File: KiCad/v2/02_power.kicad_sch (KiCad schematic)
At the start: 1 part, among them IC201 TPS63000DRCR

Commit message: scheme for voltage regulators
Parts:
- added C201, C202, C208, C209: 2.2uF, Capacitor_SMD:C_0603_1608Metric, symbol Device:C
- added C203, C205, C206, C210, C212, C213: 10uF, Capacitor_SMD:C_0603_1608Metric, symbol Device:C
- added C204, C211: 30pF, Capacitor_SMD:C_0603_1608Metric, symbol Device:C
- added C207, C214: 100nF, Capacitor_SMD:C_0603_1608Metric, symbol Device:C
- added C215, C216: 22uF, Capacitor_SMD:C_0603_1608Metric, symbol Device:C
- added D201, D203, D205, D206: 1N5819HW-7-F, Diode_SMD:D_SOD-123, symbol Device:D_Schottky
- added D202, D204: LED, LED_SMD:LED_0603_1608Metric, symbol Device:LED
- added F201, F202: 3A, Fuse:Fuse_0805_2012Metric, symbol Device:Polyfuse
- added FB201, FB202: 120R, Fuse:Fuse_0603_1608Metric, symbol Device:FerriteBead
- added IC202: TPS63000DRCR, psu:TPS63002DRCR, symbol psu:TPS63000DRCR
- added J201: Barrel_Jack_Switch_Pin3Ring, Connector_BarrelJack:BarrelJack_GCT_DCJ200-10-A_Horizontal, symbol Connector:Barrel_Jack_Switch_Pin3Ring
- added J202, J204: Conn_01x03_Pin, Connector_PinHeader_2.54mm:PinHeader_1x03_P2.54mm_Vertical, symbol Connector:Conn_01x03_Pin
- added J203, J205: Conn_02x03_Odd_Even, Connector_PinHeader_2.54mm:PinHeader_2x03_P2.54mm_Vertical, symbol Connector_Generic:Conn_02x03_Odd_Even
- added L201, L202: 2u2H, Inductor_SMD:L_Changjiang_FXL0630, symbol Device:L
- added R201, R205: 1kR, Resistor_SMD:R_0402_1005Metric, symbol Device:R
- added R202, R206: 100R, Resistor_SMD:R_0402_1005Metric, symbol Device:R
- added R203: 900kR, Resistor_SMD:R_0402_1005Metric, symbol Device:R
- added R204, R208: 100kR, Resistor_SMD:R_0402_1005Metric, symbol Device:R
- added R207: 560kR, Resistor_SMD:R_0402_1005Metric, symbol Device:R
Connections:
- net +5V: now reaches IC201.1 (VOUT)
- net +5V: now also C204.1, C205.1, C206.1, J202.1 (Pin_1), J204.1 (Pin_1), R201.2, R203.1
- net 5V_FB: now reaches IC201.10 (FB)
- net 5V_FB: now also C204.2, R203.2, R204.1
- net GND: now reaches IC201.11 (EP_1)
- net GND: now also IC201.12 (EP_2), IC201.13 (EP_3), IC201.14 (EP_4), IC201.15 (EP_5), IC201.3 (PGND), IC201.9 (GND), C201.2, C202.2, C203.2, C205.2, C206.2, C207.2, C208.2, C209.2, C210.2, C212.2, C213.2, C214.2, C215.2, C216.2, D202.1 (K), D204.1 (K), IC202.11 (EP_1), IC202.12 (EP_2), IC202.13 (EP_3), IC202.14 (EP_4), IC202.15 (EP_5), IC202.3 (PGND), IC202.9 (GND), J201.2, J201.3, J203.2 (Pin_2), J203.4 (Pin_4), J203.6 (Pin_6), J205.2 (Pin_2), J205.4 (Pin_4), J205.6 (Pin_6), R204.2, R208.2
- net at IC201.2 (L2): now also L201.2
- net at IC201.4 (L1): now also L201.1
- net +5V_IN: now reaches IC201.5 (VIN)
- net +5V_IN: now also C203.1, C210.1, D201.1 (K), D203.1 (K), IC202.5 (VIN), R202.1, R206.1
- net 5V_IN_EN: now reaches IC201.6 (EN)
- net 5V_IN_EN: now also IC201.7 (PS/SYNC), IC201.8 (VINA), C207.1, R202.2
- new net: D205.2 (A), J202.2 (Pin_2)
- new net: D206.2 (A), J204.2 (Pin_2)
- new net: D202.2 (A), R201.1
- new net: D204.2 (A), R205.1
- new net: IC202.4 (L1), L202.1
- new net: IC202.2 (L2), L202.2
- new net +3V3: C211.1, C212.1, C213.1, IC202.1 (VOUT), J202.3 (Pin_3), J204.3 (Pin_3), R205.2, R207.1
- new net +5V_BJ: F202.1, J201.1
- new net +5V_IN_FILT: C209.1, D203.2 (A), FB202.1
- new net +5V_IN_FUSE: C208.1, F202.2, FB202.2
- new net 3V3_FB: C211.2, IC202.10 (FB), R207.2, R208.1
- new net 3V3_IN_EN: C214.1, IC202.6 (EN), IC202.7 (PS/SYNC), IC202.8 (VINA), R206.2
- new net VBUS_CONN: F201.1
- new net VCC_L: C215.1, D205.1 (K), D206.1 (K), J203.1 (Pin_1), J203.3 (Pin_3), J203.5 (Pin_5)
- new net VCC_R: C216.1, J205.1 (Pin_1), J205.3 (Pin_3), J205.5 (Pin_5)
- new net VUSB: C201.1, F201.2, FB201.2
- new net VUSB_FILT: C202.1, D201.2 (A), FB201.1
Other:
- note added: "Input filters"
- note added: "Power out pins"
- note added: "Voltage regulators"
- note added: "[2] Power"
- moved on the sheet: IC201

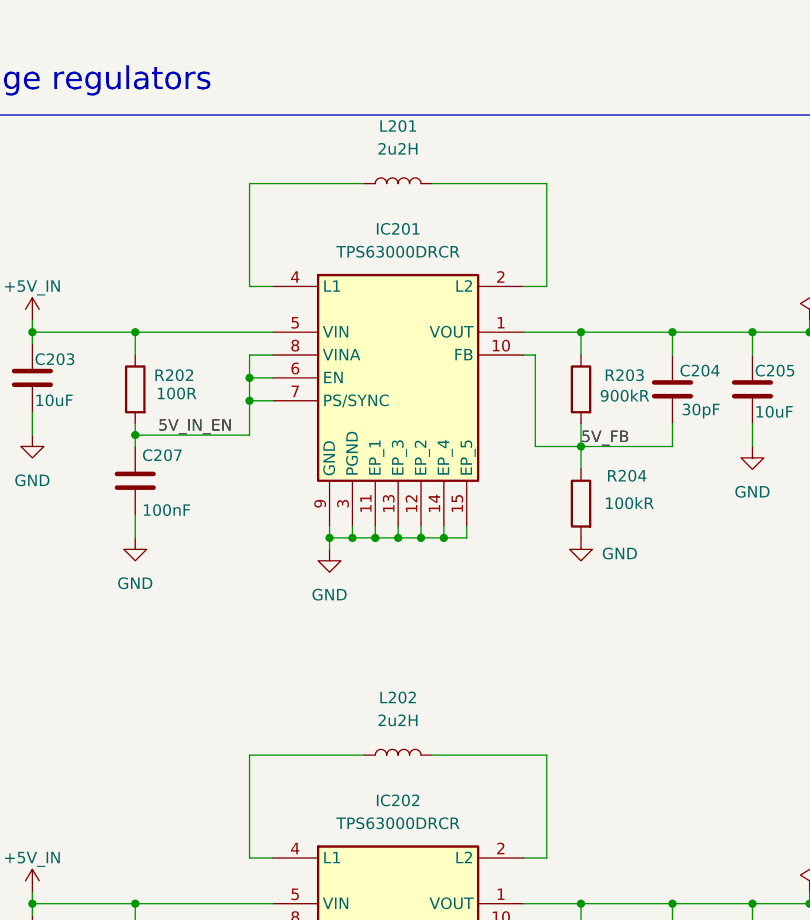
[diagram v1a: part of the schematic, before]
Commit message: Update USB connection scheme
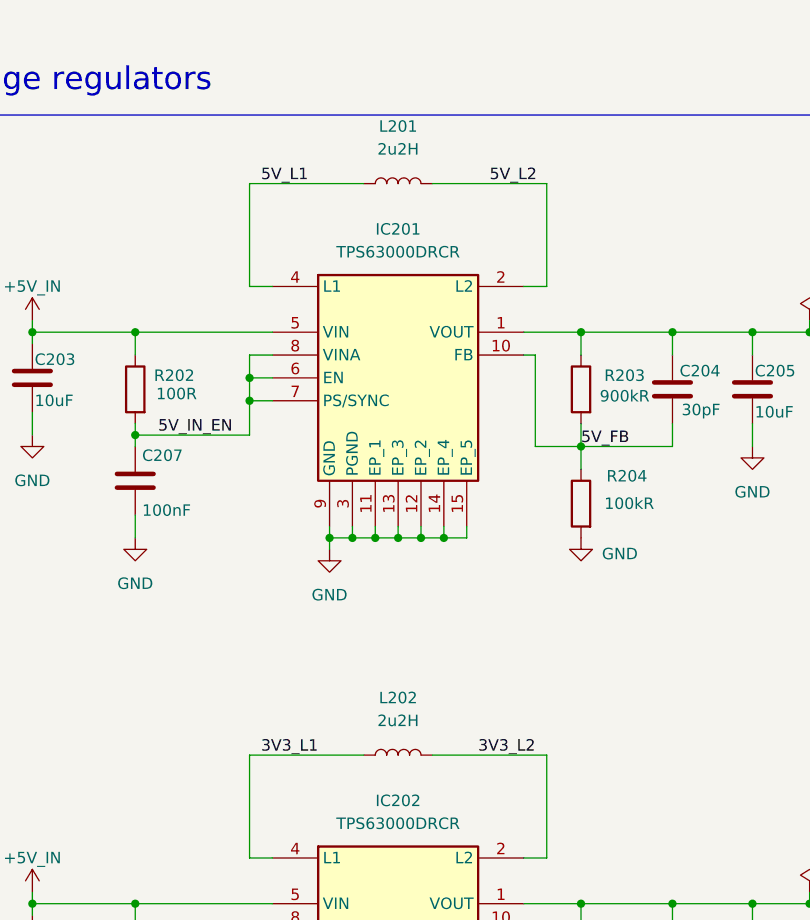
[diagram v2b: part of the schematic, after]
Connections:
- net 5V_L2: now reaches IC201.2 (L2), L201.2
- net 5V_L1: now reaches IC201.4 (L1), L201.1
- net 3V3_L1: now reaches IC202.4 (L1), L202.1
- net 3V3_L2: now reaches IC202.2 (L2), L202.2
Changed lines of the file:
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@@
+		)
+	)
+	(label "5V_L1"
+		(at 177.8 34.29 0)
+		(effects
+			(font
+				(size 1.27 1.27)
+			)
+			(justify left bottom)
 		)
 	)
 	(label "3V3_IN_EN"
 		(at 166.37 125.73 0)
+		(effects
+			(font
+				(size 1.27 1.27)
+			)
+			(justify left bottom)
+		)
+	)
+	(label "5V_L2"
+		(at 203.2 34.29 0)
+		(effects
+			(font
+				(size 1.27 1.27)
+			)
+			(justify left bottom)
+		)
+	)
+	(label "3V3_L1"
+		(at 177.8 97.79 0)
 		(effects
 			(font
@@
 		(effects
 			(font
+				(size 1.27 1.27)
+			)
+			(justify left bottom)
+		)
+	)
+	(label "3V3_L2"
+		(at 201.93 97.79 0)
+		(effects
+			(font

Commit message: Scheme updates
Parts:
- added FB202, FB204: 120R, Fuse:Fuse_0603_1608Metric, symbol Device:FerriteBead
- renumbered FB202 to FB203
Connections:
- net +3V3: now also FB204.1; no longer C211.1, C212.1, C213.1, IC202.1 (VOUT), R207.1
- net +5V: now also FB202.1; no longer C204.1, C205.1, C206.1, IC201.1 (VOUT), R203.1
- new net 3V3_OUT: C211.1, C212.1, C213.1, FB204.2, IC202.1 (VOUT), R207.1
- new net 5V_OUT: C204.1, C205.1, C206.1, FB202.2, IC201.1 (VOUT), R203.1
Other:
- note added: "R1/R2 = Vout/Vfb - 1 = 3.3V/0.5V-1 = 6.6-1 = 5.6 Values 560kR and 100kR are OK."
- note added: "When the output voltage is regulated properly, the typical value of the voltage at the FB pin is 500 mV. R1 = R2 * (Vout/Vfb - 1) R1/R2 = Vout/Vfb - 1 = 5V/0.5V-1 = 10-1 = 9 Values 900kR and 100kR are OK."
- moved on the sheet: D202, D204, R201, R205

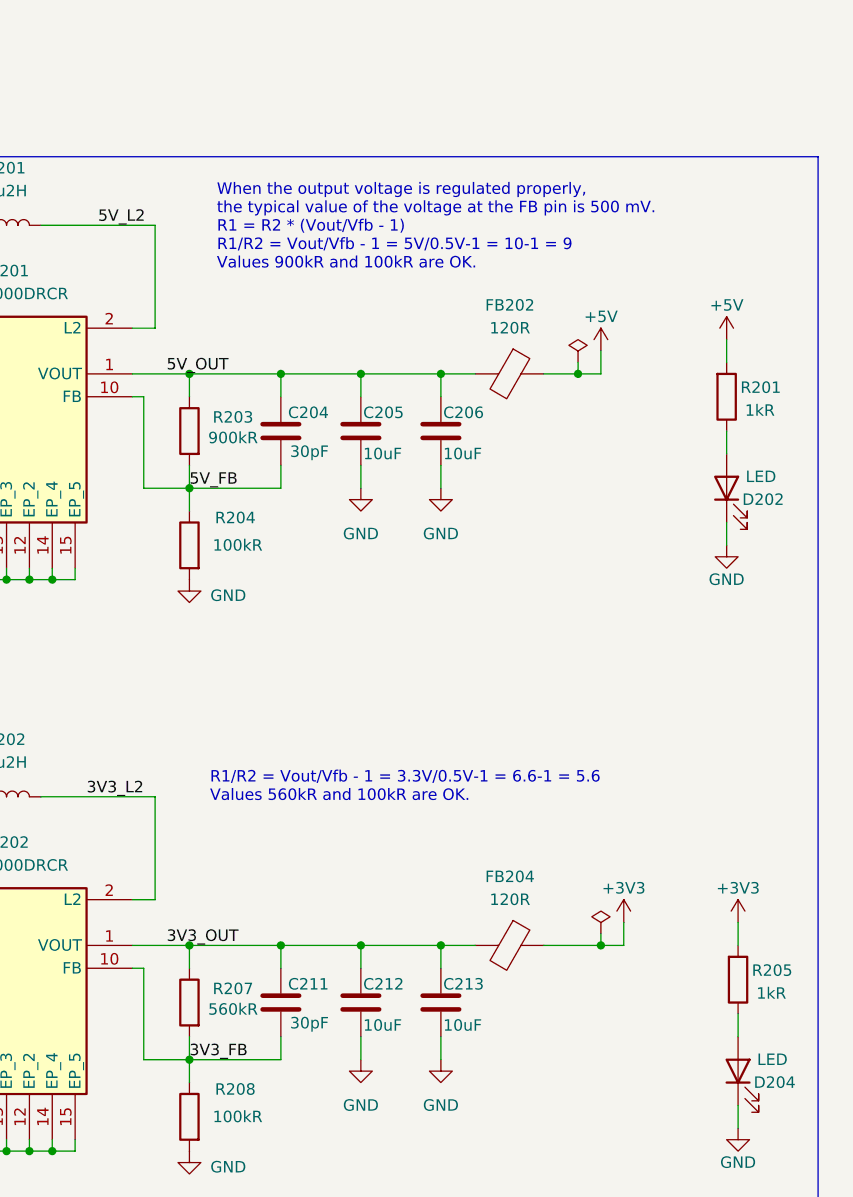
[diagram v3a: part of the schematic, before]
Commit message: update FB capacitors
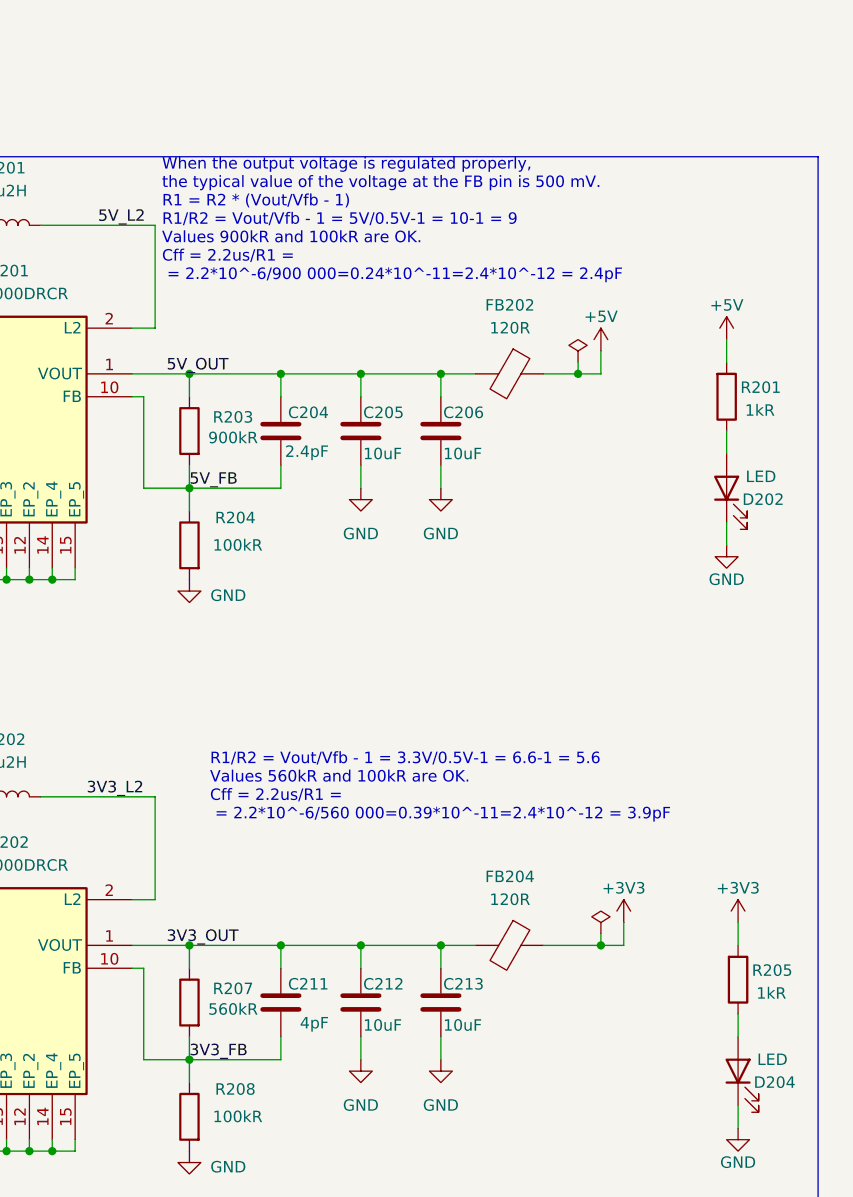
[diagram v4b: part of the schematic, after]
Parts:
- C204: value 30pF -> 2.4pF
- C211: value 30pF -> 4pF
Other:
- note added: "R1/R2 = Vout/Vfb - 1 = 3.3V/0.5V-1 = 6.6-1 = 5.6 Values 560kR and 100kR are OK. Cff = 2.2us/R1 = = 2.2*10^-6/560 000=0.39*10^-11=2.4*10^-12 = 3.9pF"
- note added: "When the output voltage is regulated properly, the typical value of the voltage at the FB pin is 500 mV. R1 = R2 * (Vout/Vfb - 1) R1/R2 = Vout/Vfb - 1 = 5V/0.5V-1 = 10-1 = 9 Values 900kR and 100kR are OK. Cff = 2.2us/R1 = = 2.2*10^-6/900 000=0.24*10^-11=2.4*10^-12 = 2.4pF"
- note removed: "R1/R2 = Vout/Vfb - 1 = 3.3V/0.5V-1 = 6.6-1 = 5.6 Values 560kR and 100kR are OK."
- note removed: "When the output voltage is regulated properly, the typical value of the voltage at the FB pin is 500 mV. R1 = R2 * (Vout/Vfb - 1) R1/R2 = Vout/Vfb - 1 = 5V/0.5V-1 = 10-1 = 9 Values 900kR and 100kR are OK."
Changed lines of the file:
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@@
 		)
 	)
-	(text "When the output voltage is regulated properly, \nthe typical value of the voltage at the FB pin is 500 mV.\nR1 = R2 * (Vout/Vfb - 1)\nR1/R2 = Vout/Vfb - 1 = 5V/0.5V-1 = 10-1 = 9\nValues 900kR and 100kR are OK."
+	(text "When the output voltage is regulated properly, \nthe typical value of the voltage at the FB pin is 500 mV.\nR1 = R2 * (Vout/Vfb - 1)\nR1/R2 = Vout/Vfb - 1 = 5V/0.5V-1 = 10-1 = 9\nValues 900kR and 100kR are OK.\nCff = 2.2us/R1 = \n = 2.2*10^-6/900 000=0.24*10^-11=2.4*10^-12 = 2.4pF"
 		(exclude_from_sim no)
-		(at 216.408 34.544 0)
+		(at 210.312 33.782 0)
 		(effects
 			(font
@@
 		)
 	)
-	(text "R1/R2 = Vout/Vfb - 1 = 3.3V/0.5V-1 = 6.6-1 = 5.6\nValues 560kR and 100kR are OK."
+	(text "R1/R2 = Vout/Vfb - 1 = 3.3V/0.5V-1 = 6.6-1 = 5.6\nValues 560kR and 100kR are OK.\nCff = 2.2us/R1 = \n = 2.2*10^-6/560 000=0.39*10^-11=2.4*10^-12 = 3.9pF"
 		(exclude_from_sim no)
 		(at 215.646 96.774 0)
@@
 			)
 		)
-		(property "Value" "30pF"
+		(property "Value" "4pF"
 			(at 228.854 122.936 0)
 			(effects
@@
 			)
 		)
-		(property "Value" "30pF"
+		(property "Value" "2.4pF"
 			(at 228.854 59.436 0)
 			(effects

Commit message: Initial components placement
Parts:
- removed J201: Barrel_Jack_Switch_Pin3Ring, Connector_BarrelJack:BarrelJack_GCT_DCJ200-10-A_Horizontal, symbol Connector:Barrel_Jack_Switch_Pin3Ring
- added J201: Conn_01x02_Pin, Connector_PinHeader_2.54mm:PinHeader_1x02_P2.54mm_Vertical, symbol Connector:Conn_01x02_Pin
- C204, C211: now not fitted
- C207, C214: footprint Capacitor_SMD:C_0603_1608Metric -> Capacitor_SMD:C_0402_1005Metric
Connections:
- net +5V_BJ: now also J201.1 (Pin_1)
- net GND: now also J201.2 (Pin_2)
- net VCC_L: no longer D206.1 (K)
- net VCC_R: now also D206.1 (K)
